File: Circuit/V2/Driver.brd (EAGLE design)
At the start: 58.8 x 53.6 mm, 36 parts

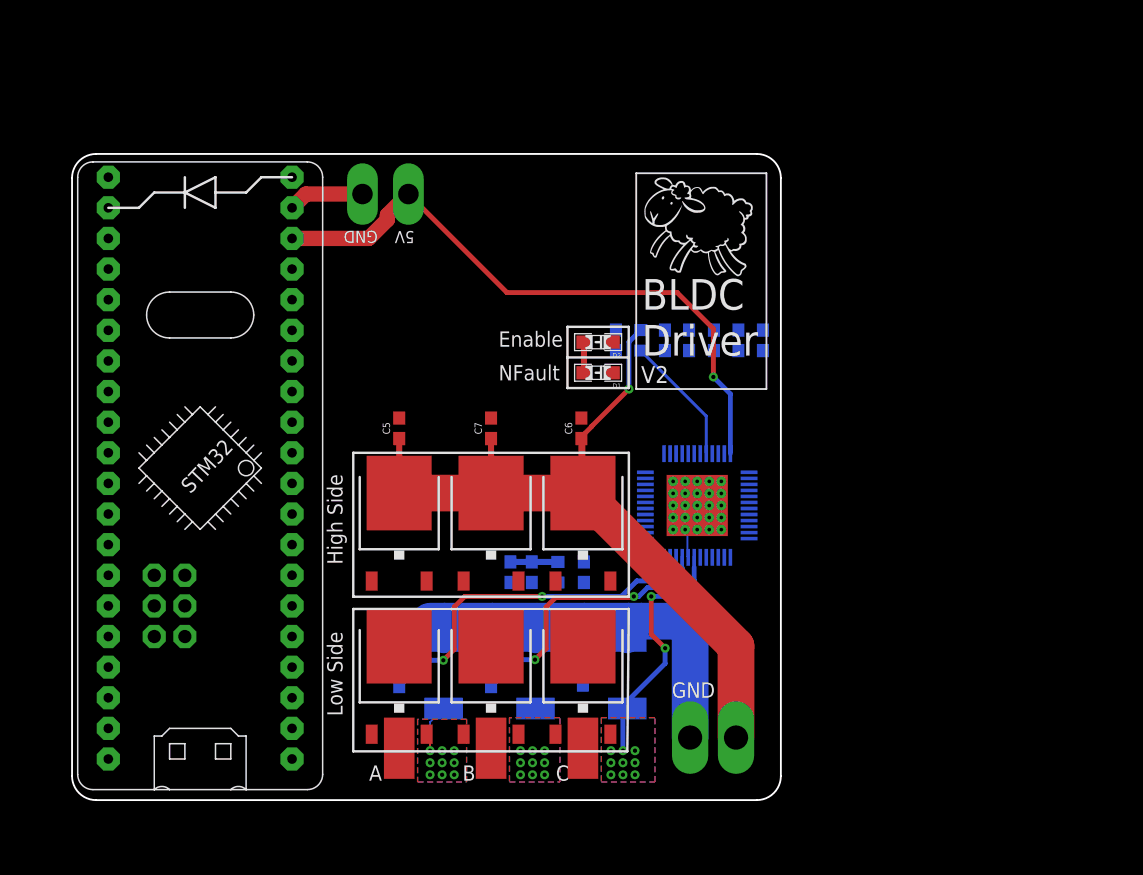
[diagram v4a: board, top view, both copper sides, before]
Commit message: Mirror the PCB arrangement
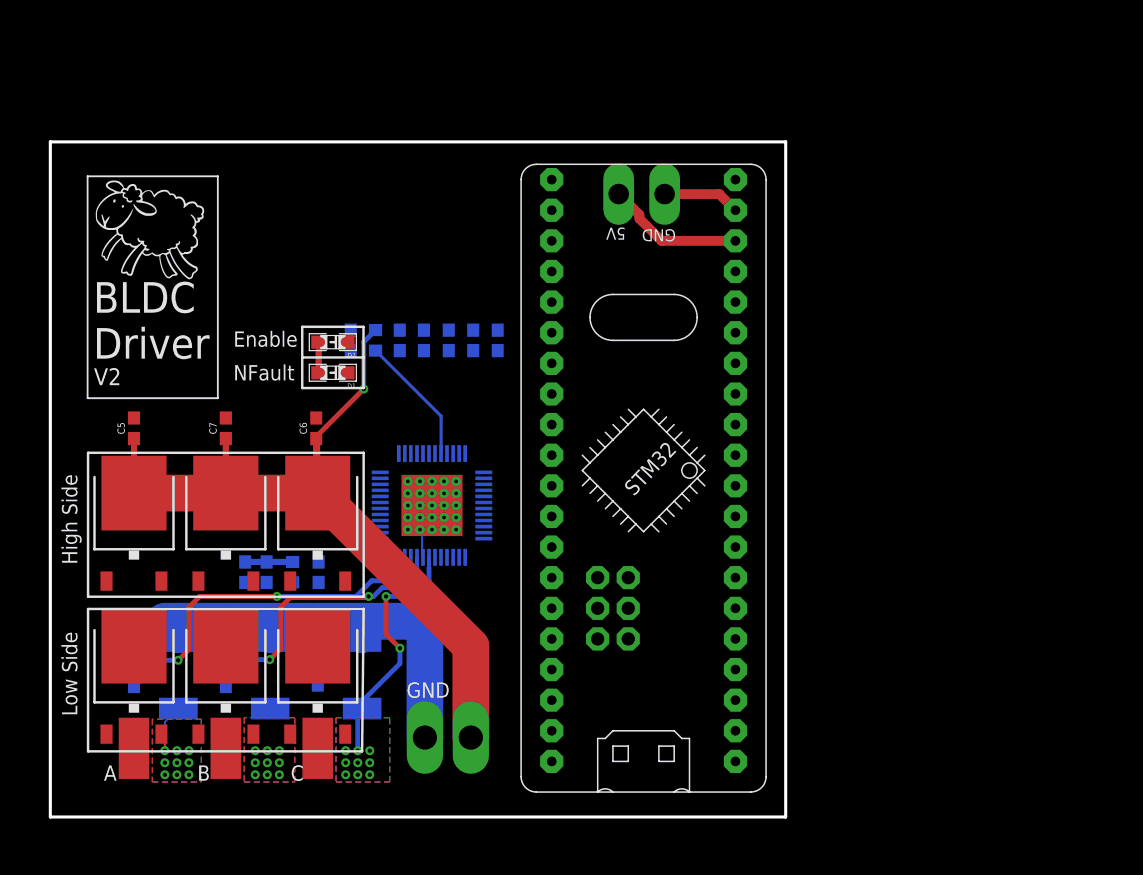
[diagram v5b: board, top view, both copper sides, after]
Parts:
- moved U$1 36.8 mm to (45.7, 34.1)
- moved C1 22.0 mm to (21.3, 19.3)
- moved C13 22.0 mm to (30.0, 38.5)
- moved R2 22.0 mm to (17.2, 10.8)
- moved A 22.0 mm to (5.94, 4.70)
- moved B 22.0 mm to (13.6, 4.70)
- moved C 22.0 mm to (21.2, 4.70)
- moved C10 22.0 mm to (36.1, 38.5)
- moved C11 22.0 mm to (32.0, 38.5)
- moved C12 22.0 mm to (34.1, 38.5)
- moved C14 22.0 mm to (23.9, 38.5)
- moved C15 22.0 mm to (28.0, 38.5)
- moved C2 22.0 mm to (5.94, 10.7)
- moved C3 22.0 mm to (13.6, 10.7)
- moved C4 22.0 mm to (21.2, 10.8)
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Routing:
- net VCC: track 56.4 -> 15.7 mm, vias 1 -> 0
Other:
- board size 58.8 x 53.6 mm -> 61 x 56 mm

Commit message: Delete some resistors and capacitors value in Tvalue and Bvalue layers
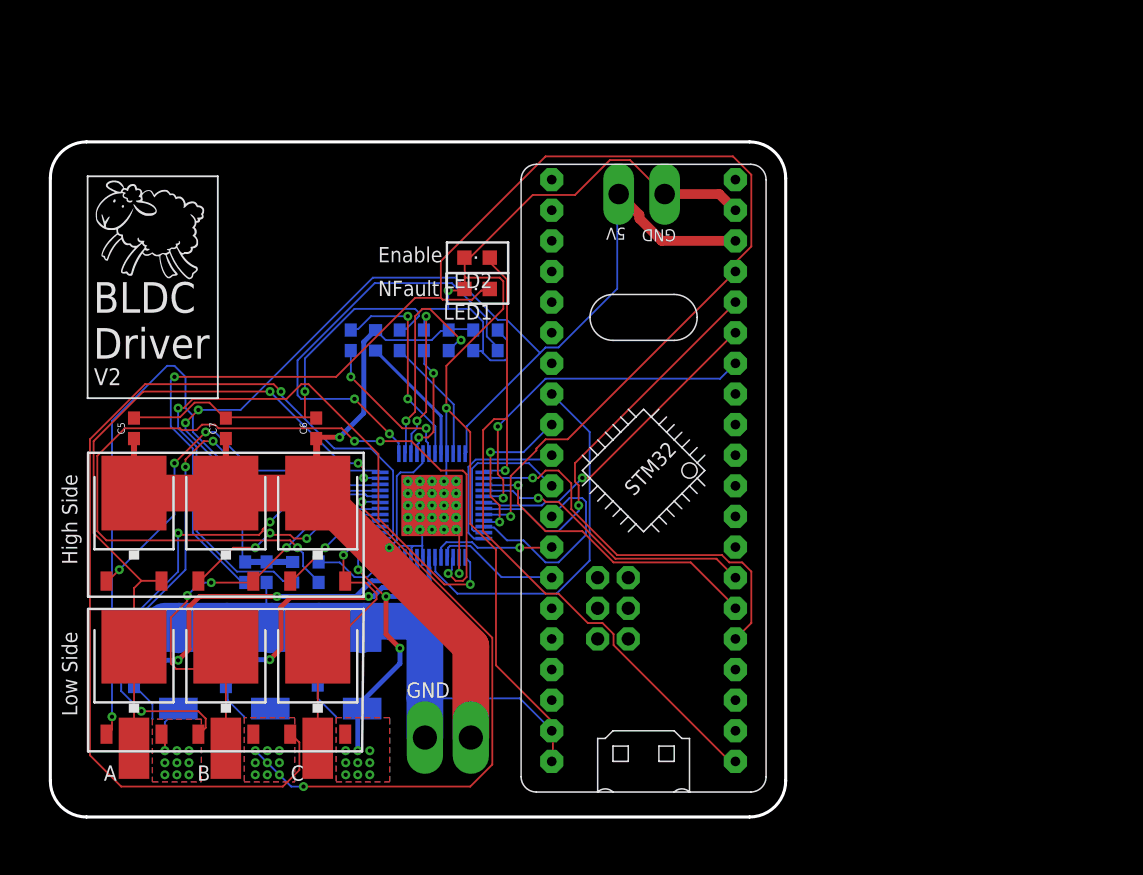
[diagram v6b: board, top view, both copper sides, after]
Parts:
- removed D1, D2: (no value), standardparts:0805.LED
- added LED1, LED2: (no value), led:CHIPLED_0805
- turned C14 to 90 degrees
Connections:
- net GND: now also LED1.C, LED2.C; no longer D1.P$2, D2.P$2
- net PB12: now also LED2.A; no longer D2.P$1
- net PB9: now also LED1.A; no longer D1.P$1
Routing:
- net GND: track 88.9 -> 274.0 mm, vias 0 -> 4
- net PB9: track 0.00 -> 122.2 mm, vias 0 -> 2
- net GL_C: track 0.00 -> 85.3 mm, vias 0 -> 1
- net VCC: track 15.7 -> 93.7 mm, vias 0 -> 2
- net N$15: track 0.00 -> 72.5 mm, vias 0 -> 4
- net PB12: track 0.00 -> 60.3 mm, vias 0 -> 1
- net PWRGD: track 0.00 -> 58.1 mm, vias 0 -> 2
- net SH_A: track 0.00 -> 57.9 mm, vias 0 -> 3
- net GL_A: track 0.00 -> 57.0 mm, vias 0 -> 1
- net SN2: track 22.9 -> 75.6 mm, vias 11 -> 13
- net GL_B: track 0.00 -> 43.0 mm, vias 0 -> 3
- net SN1: track 35.1 -> 78.0 mm, vias 11 -> 13
- net SH_B: track 0.00 -> 40.3 mm, vias 0 -> 3
- net VCP_LSD: track 0.00 -> 36.4 mm, vias 0 -> 2
- net PA8: track 0.00 -> 33.3 mm, vias 0 -> 1
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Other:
- outline, holes or cut-outs redrawn
